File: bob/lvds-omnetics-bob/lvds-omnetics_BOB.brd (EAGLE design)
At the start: 43.7 x 25.7 mm, 34 parts, among them U1 SN65LVDS1, U2 SN65LVDS2, U3 SN65LVDS1, U4 SN65LVDS2, U5 SN65LVDS1, U6 SN65LVDS1

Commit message: Many final changes to design before fabrication.
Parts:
- C1: value 0.1uF -> 10uF; device puggleboard:0603 -> puggleboard:0805
- C13: value 10uF -> 1nF; device puggleboard:0805 -> puggleboard:0603
- C7: value 1nF -> 0.1uF
- R1: value 100 -> 1k
- R2: value 100 -> 0
- R8: value 0 -> 100
- R9: value 1k -> 100
- moved C13 25.5 mm to (19.9, 3.56), turned to 270 degrees
- moved R2 17.3 mm to (10.3, 21.3), turned to 180 degrees
- moved C7 16.9 mm to (18.4, 3.56)
- moved R8 15.1 mm to (25.1, 20.1), turned to 270 degrees
- moved R4 11.8 mm to (10.3, 13.7)
- moved R6 11.8 mm to (10.3, 6.10)
- moved C11 11.6 mm to (19.9, 11.2)
- moved C3 11.6 mm to (18.4, 18.8)
- moved C5 11.6 mm to (18.4, 11.2)
- moved C9 11.6 mm to (19.9, 18.8)
- moved R1 10.4 mm to (30.4, 11.0), turned to 0 degrees
- moved C2 9.02 mm to (9.53, 18.8)
- moved C4 9.02 mm to (9.53, 11.2)
- moved C6 9.02 mm to (9.53, 3.56)
- moved C10 9.02 mm to (11.0, 11.2)
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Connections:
- removed net VDRIVE: C1.1, C10.1, C11.1, C12.1, C13.1, C2.1, C3.1, C4.1, C5.1, C6.1, C7.1, C8.1, C9.1, D_I/O.1, HS_A.B6, HS_B.B6, R9.1, U1.1, U2.1, U3.1, U4.1, U5.1, U6.1
- new net VCC: C1.1, C10.1, C11.1, C12.1, C13.1, C2.1, C3.1, C4.1, C5.1, C6.1, C7.1, C8.1, C9.1, D_I/O.1, HS_A.B6, HS_B.B6, R1.1, U1.1, U2.1, U3.1, U4.1, U5.1, U6.1
- net CS1: now also R4.2; no longer R5.2
- net CS2: now also R6.2; no longer R7.2
- net MISO1: now also R3.2; no longer R4.2
- net MISO1_N: now also R8.2; no longer R1.2
- net MISO1_P: now also R8.1; no longer R1.1
- net MISO2: now also R5.2; no longer R6.2
- net MISO2_N: now also R9.2; no longer R2.2
- net MISO2_P: now also R9.1; no longer R2.1
- net MOSI: now also R7.2; no longer R8.2
- net N$2: now also R3.1; no longer R4.1
- net N$3: now also R4.1; no longer R5.1
- net N$4: now also R5.1; no longer R6.1
- net N$5: now also R6.1; no longer R7.1
- net N$6: now also R7.1; no longer R8.1
- net N$7: now also R2.1; no longer R3.1
- net N$9: now also R1.2; no longer R9.2
- net SCLK: now also R2.2; no longer R3.2
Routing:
- net VDRIVE: track 33.5 -> 0.00 mm, vias 11 -> 0
- net VCC: track 0.00 -> 33.2 mm, vias 0 -> 11
- net GND: track 40.1 -> 40.7 mm
- added copper zone on layer 15, net VCC
- removed copper zone on layer 15, net VDRIVE
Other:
- board text added: "LVDS-Omnetics-BOB v1.0, Aug. 2013"
- board text removed: "LVDS-Omnetics-BOB v1.0"

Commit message: Tenative fabricaiton ready v2.0. Will tag upon recieving the goods.
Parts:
- added U$2: (no value), ohw-logo:OSHW_FILLX500_NOTEXT
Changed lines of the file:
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@@
 <layer number="22" name="bPlace" color="7" fill="1" visible="yes" active="yes"/>
 <layer number="23" name="tOrigins" color="15" fill="1" visible="yes" active="yes"/>
-<layer number="24" name="bOrigins" color="15" fill="1" visible="no" active="yes"/>
+<layer number="24" name="bOrigins" color="15" fill="1" visible="yes" active="yes"/>
 <layer number="25" name="tNames" color="7" fill="1" visible="yes" active="yes"/>
 <layer number="26" name="bNames" color="7" fill="1" visible="no" active="yes"/>
@@
 <wire x1="42.96958125" y1="25.654" x2="0.762" y2="25.654" width="0" layer="20"/>
 <wire x1="0.762" y1="25.654" x2="0" y2="24.850784375" width="0" layer="20" curve="90"/>
-<text x="33.528" y="4.318" size="0.8128" layer="21" font="vector" align="center">LVDS-Omnetics-BOB
+<text x="33.528" y="2.921" size="0.8128" layer="21" font="vector" align="center">LVDS-Omnetics-BOB
 v1.0, Aug. 2013</text>
 <text x="42.672" y="1.524" size="0.7112" layer="22" font="vector" rot="MR0">S/N:</text>
@@
 <attribute name="VALUE" x="28.956" y="12.319" size="0.7366" layer="27" font="vector" ratio="10" align="center-left"/>
 </element>
+<element name="U$2" library="ohw-logo" package="OSHW_FILLX500_NOTEXT" value="" x="39.243" y="4.064" rot="MR0"/>
 </elements>
 <signals>

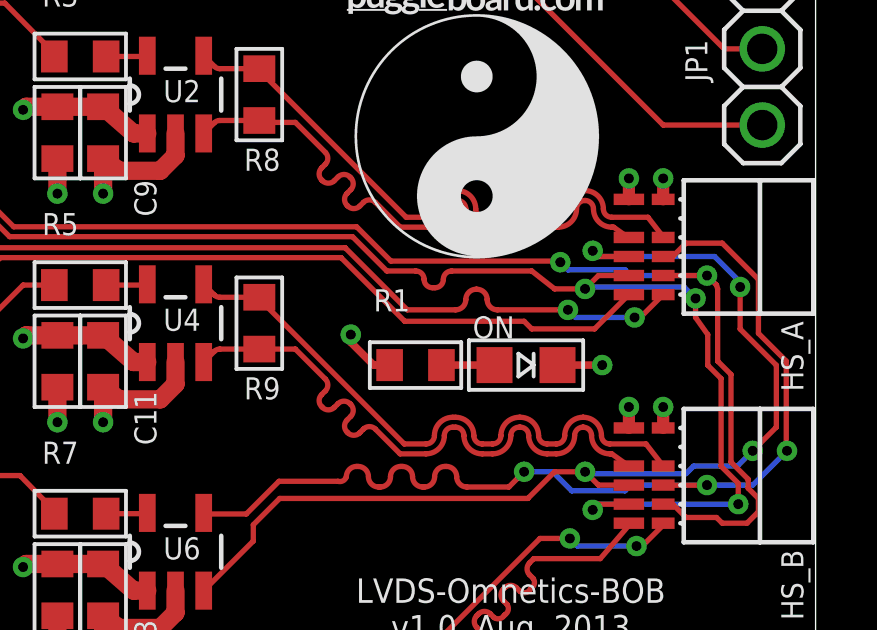
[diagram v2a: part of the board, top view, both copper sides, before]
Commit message: Finished BOMs (and integrated parts into database) for all the BOBs. Now must do for the main board. Will take a while.
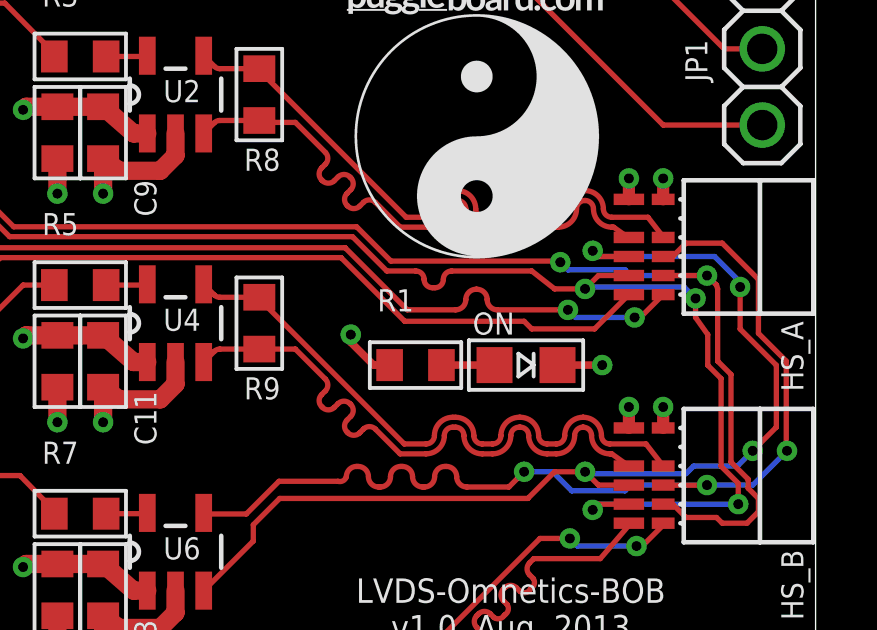
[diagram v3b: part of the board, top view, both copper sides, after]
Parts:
- D_I/O: value PINHD-2X8VERT -> PINHD-2X8FEMALEVERT; device adafruit:2X08 -> puggleboard:2X08
- JP1: value (none) -> 1X03HEADER; device adafruit:1X03 -> puggleboard:1X03
- ON: value (none) -> LEDGREEN_0805
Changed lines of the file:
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@@
 <attribute name="NAME" x="24.638" y="17.526" size="0.7366" layer="25" font="vector"/>
 <attribute name="VALUE" x="24.638" y="16.51" size="0.7366" layer="27" font="vector"/>
+<attribute name="MN" value="Panasonic" x="25.146" y="20.066" size="1.778" layer="27" rot="R270" display="off"/>
+<attribute name="DK" value="PxxxxHTR-ND" x="25.146" y="20.066" size="1.778" layer="27" rot="R270" display="off"/>
+<attribute name="MPN" value="ERJ-3EKFxxxxV" x="25.146" y="20.066" size="1.778" layer="27" rot="R270" display="off"/>
 </element>
 <element name="U5" library="ti-extended" package="SOT95P280X145-5N" value="SN65LVDS1" x="13.462" y="4.826" smashed="yes" rot="R90">
@@
 <attribute name="NAME" x="24.638" y="9.906" size="0.7366" layer="25" font="vector"/>
 <attribute name="VALUE" x="24.511" y="8.89" size="0.7366" layer="27" font="vector"/>
+<attribute name="MN" value="Panasonic" x="25.146" y="12.446" size="1.778" layer="27" rot="R270" display="off"/>
+<attribute name="DK" value="PxxxxHTR-ND" x="25.146" y="12.446" size="1.778" layer="27" rot="R270" display="off"/>
+<attribute name="MPN" value="ERJ-3EKFxxxxV" x="25.146" y="12.446" size="1.778" layer="27" rot="R270" display="off"/>
 </element>
-<element name="D_I/O" library="adafruit" package="2X08" value="PINHD-2X8VERT" x="3.048" y="11.176" smashed="yes" rot="R270">
+<element name="D_I/O" library="puggleboard" package="2X08" value="PINHD-2X8FEMALEVERT" x="3.048" y="11.176" smashed="yes" rot="R270">
 <attribute name="NAME" x="5.715" y="12.446" size="0.7366" layer="25" font="vector" ratio="10" rot="R270"/>
+<attribute name="MN" value="Sullins" x="3.048" y="11.176" size="1.778" layer="27" rot="R270" display="off"/>
+<attribute name="DK" value="S7111-ND" x="3.048" y="11.176" size="1.778" layer="27" rot="R270" display="off"/>
+<attribute name="MPN" value="PPPC082LFBN-RC" x="3.048" y="11.176" size="1.778" layer="27" rot="R270" display="off"/>
 </element>
 <element name="C1" library="puggleboard" package="0805" value="10uF" x="3.048" y="22.606" smashed="yes">
 <attribute name="NAME" x="5.08" y="24.384" size="0.7366" layer="25" font="vector"/>
 <attribute name="VALUE" x="5.08" y="23.368" size="0.7366" layer="27" font="vector"/>
+<attribute name="MN" value="TDK Corp." x="3.048" y="22.606" size="1.778" layer="27" display="off"/>
+<attribute name="PARTNO" value="C2012X5R1Cxxxxxxx" x="3.048" y="22.606" size="1.778" layer="27" display="off"/>
+<attribute name="DK" value="" x="3.048" y="22.606" size="1.778" layer="27" display="off"/>
+<attribute name="VID" value="DK" x="3.048" y="22.606" size="1.778" layer="27" display="off"/>
 </element>
 <element name="HS_A" library="puggleboard" package="OMNETICS_PZN_12_AA-SINGLEBUS" value="RHD2000-CABLE-DAQ-SIDE-SINGLE" x="40.894" y="14.986" smashed="yes" rot="R270">
@@
 <attribute name="NAME" x="9.017" y="23.368" size="0.7366" layer="25" font="vector" ratio="10" rot="R180" align="center-right"/>
 <attribute name="VALUE" x="9.017" y="22.606" size="0.7366" layer="27" font="vector" ratio="10" align="center-left"/>
+<attribute name="MN" value="Panasonic" x="10.287" y="21.336" size="1.778" layer="27" rot="R180" display="off"/>
+<attribute name="DK" value="PxxxxHTR-ND" x="10.287" y="21.336" size="1.778" layer="27" rot="R180" display="off"/>
+<attribute name="MPN" value="ERJ-3EKFxxxxV" x="10.287" y="21.336" size="1.778" layer="27" rot="R180" display="off"/>
 </element>
 <element name="R3" library="puggleboard" package="0603" value="0" x="19.177" y="21.336" smashed="yes" rot="R180">
 <attribute name="NAME" x="17.907" y="23.368" size="0.7366" layer="25" font="vector" ratio="10" rot="R180" align="center-right"/>
 <attribute name="VALUE" x="17.907" y="22.606" size="0.7366" layer="27" font="vector" ratio="10" align="center-left"/>
+<attribute name="MN" value="Panasonic" x="19.177" y="21.336" size="1.778" layer="27" rot="R180" display="off"/>
+<attribute name="DK" value="PxxxxHTR-ND" x="19.177" y="21.336" size="1.778" layer="27" rot="R180" display="off"/>
+<attribute name="MPN" value="ERJ-3EKFxxxxV" x="19.177" y="21.336" size="1.778" layer="27" rot="R180" display="off"/>
 </element>
 <element name="R4" library="puggleboard" package="0603" value="0" x="10.287" y="13.716" smashed="yes" rot="R180">
 <attribute name="NAME" x="9.017" y="15.748" size="0.7366" layer="25" font="vector" ratio="10" rot="R180" align="center-right"/>
 <attribute name="VALUE" x="9.017" y="14.986" size="0.7366" layer="27" font="vector" ratio="10" align="center-left"/>
+<attribute name="MN" value="Panasonic" x="10.287" y="13.716" size="1.778" layer="27" rot="R180" display="off"/>
+<attribute name="DK" value="PxxxxHTR-ND" x="10.287" y="13.716" size="1.778" layer="27" rot="R180" display="off"/>
+<attribute name="MPN" value="ERJ-3EKFxxxxV" x="10.287" y="13.716" size="1.778" layer="27" rot="R180" display="off"/>
 </element>
 <element name="R5" library="puggleboard" package="0603" value="0" x="19.177" y="13.716" smashed="yes" rot="R180">
 <attribute name="NAME" x="17.907" y="15.748" size="0.7366" layer="25" font="vector" ratio="10" rot="R180" align="center-right"/>
 <attribute name="VALUE" x="17.907" y="14.986" size="0.7366" layer="27" font="vector" ratio="10" align="center-left"/>
+<attribute name="MN" value="Panasonic" x="19.177" y="13.716" size="1.778" layer="27" rot="R180" display="off"/>
+<attribute name="DK" value="PxxxxHTR-ND" x="19.177" y="13.716" size="1.778" layer="27" rot="R180" display="off"/>
+<attribute name="MPN" value="ERJ-3EKFxxxxV" x="19.177" y="13.716" size="1.778" layer="27" rot="R180" display="off"/>
 </element>
 <element name="R6" library="puggleboard" package="0603" value="0" x="10.287" y="6.096" smashed="yes" rot="R180">
 <attribute name="NAME" x="9.017" y="8.128" size="0.7366" layer="25" font="vector" ratio="10" rot="R180" align="center-right"/>
 <attribute name="VALUE" x="9.017" y="7.366" size="0.7366" layer="27" font="vector" ratio="10" align="center-left"/>
+<attribute name="MN" value="Panasonic" x="10.287" y="6.096" size="1.778" layer="27" rot="R180" display="off"/>
+<attribute name="DK" value="PxxxxHTR-ND" x="10.287" y="6.096" size="1.778" layer="27" rot="R180" display="off"/>
+<attribute name="MPN" value="ERJ-3EKFxxxxV" x="10.287" y="6.096" size="1.778" layer="27" rot="R180" display="off"/>
 </element>
 <element name="R7" library="puggleboard" package="0603" value="0" x="19.177" y="6.096" smashed="yes" rot="R180">
 <attribute name="NAME" x="17.907" y="8.128" size="0.7366" layer="25" font="vector" ratio="10" rot="R180" align="center-right"/>
 <attribute name="VALUE" x="17.907" y="7.366" size="0.7366" layer="27" font="vector" ratio="10" align="center-left"/>
+<attribute name="MN" value="Panasonic" x="19.177" y="6.096" size="1.778" layer="27" rot="R180" display="off"/>
+<attribute name="DK" value="PxxxxHTR-ND" x="19.177" y="6.096" size="1.778" layer="27" rot="R180" display="off"/>
+<attribute name="MPN" value="ERJ-3EKFxxxxV" x="19.177" y="6.096" size="1.778" layer="27" rot="R180" display="off"/>
 </element>
-<element name="JP1" library="adafruit" package="1X03" value="" x="41.91" y="21.59" smashed="yes" rot="R90">
+<element name="JP1" library="puggleboard" package="1X03" value="1X03HEADER" x="41.91" y="21.59" smashed="yes" rot="R90">
 <attribute name="NAME" x="40.0812" y="20.4978" size="0.7366" layer="25" font="vector" ratio="10" rot="R90"/>
-<attribute name="VALUE" x="45.085" y="17.78" size="1.27" layer="27" rot="R90"/>
+<attribute name="MN" value="3M" x="41.91" y="21.59" size="1.778" layer="27" rot="R90" display="off"/>
+<attribute name="DK" value="3M9468-ND" x="41.91" y="21.59" size="1.778" layer="27" rot="R90" display="off"/>
+<attribute name="MPN" value="961103-5604-AR" x="41.91" y="21.59" size="1.778" layer="27" rot="R90" display="off"/>
 </element>
 <element name="U$1" library="puggleboard" package="PB-LOGO" value="" x="28.067" y="14.605"/>
-<element name="ON" library="puggleboard" package="CHIP-LED0805" value="" x="34.036" y="11.049" smashed="yes" rot="R270">
-<attribute name="NAME" x="32.258" y="11.938" size="0.7366" layer="25" font="vector"/>
-<attribute name="VALUE" x="32.766" y="8.509" size="1.27" layer="27"/>
+<element name="ON" library="puggleboard" package="CHIP-LED0805" value="LEDGREEN_0805" x="34.036" y="11.049" smashed="yes" rot="R270">
+<attribute name="NAME" x="32.258" y="12.065" size="0.7366" layer="25" font="vector"/>
+<attribute name="MN" value="598-8170-107F" x="34.036" y="11.049" size="1.778" layer="27" rot="R270" display="off"/>
+<attribute name="DK" value="350-2044-1-ND" x="34.036" y="11.049" size="1.778" layer="27" rot="R270" display="off"/>
+<attribute name="MPN" value="Dialight" x="34.036" y="11.049" size="1.778" layer="27" rot="R270" display="off"/>
 </element>
 <element name="R1" library="puggleboard" package="0603" value="1k" x="30.353" y="11.049" smashed="yes">
-<attribute name="NAME" x="28.956" y="13.208" size="0.7366" layer="25" font="vector" ratio="10" rot="R180" align="center-right"/>
-<attribute name="VALUE" x="28.956" y="12.319" size="0.7366" layer="27" font="vector" ratio="10" align="center-left"/>
+<attribute name="NAME" x="29.083" y="13.208" size="0.7366" layer="25" font="vector" ratio="10" rot="R180" align="center-right"/>
+<attribute name="VALUE" x="29.083" y="12.319" size="0.7366" layer="27" font="vector" ratio="10" align="center-left"/>
+<attribute name="MN" value="Panasonic" x="30.353" y="11.049" size="1.778" layer="27" display="off"/>
+<attribute name="DK" value="PxxxxHTR-ND" x="30.353" y="11.049" size="1.778" layer="27" display="off"/>
+<attribute name="MPN" value="ERJ-3EKFxxxxV" x="30.353" y="11.049" size="1.778" layer="27" display="off"/>
 </element>
 <element name="U$2" library="ohw-logo" package="OSHW_FILLX500_NOTEXT" value="" x="39.243" y="4.064" rot="MR0"/>
